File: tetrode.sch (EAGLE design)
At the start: 34 parts, among them IC1 MEGA8-P, J1 AVR_SPI_PROG_3X2NS, U1 LM2576T-5.0/NOPB, Y1 16MHz

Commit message: Started code
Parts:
- removed C5: 22p, resistor:C-EU025-024X044
- removed C6: 470u, resistor:CPOL-EUE5-13
- removed C7: 47u, resistor:CPOL-EUE2.5-6
- removed D2: (no value), adafruit:DIODEDO-1N4148
- removed D3: (no value), adafruit:SCHOTTKY-DIODEDO201T15
- removed L1: 100u, resistor:L-US0204/5
- removed P1, P2, P3: (no value), SparkFun-Connectors:CONN_03
- removed U1: LM2576T-5.0/NOPB, LM2576T:LM2576T-5.0/NOPB
- added J2, J3, J4: (no value), SparkFun-Connectors:CONN_05
- C1: value 47u -> 2.2u; device resistor:CPOL-EUE2.5-6 -> resistor:CPOL-EUE2-5
- C2: value 470u -> 2.2u; device resistor:CPOL-EUE5-13 -> resistor:CPOL-EUE2-5
- C4: value 22p -> 2.2u; device resistor:C-EU025-024X044 -> resistor:CPOL-EUE2-5
- Y1: value 16MHz -> (none); device SparkFun-Clocks:CRYSTAL-16MHZPTH-HC49US -> SparkFun-Clocks:RESONATORPTH-7.6X3.8
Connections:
- removed net N$5: IC1.PC2(ADC2), P3.2
- removed net N$8: D3.C, L1.2, U1.OUT
- removed net VCC: C1.+, C7.+, D2.C, U1.VIN
- net +5V: now also CN1.PWR, J2.1, J3.1, J4.1; no longer C2.+, C6.+, L1.1, P1.1, P2.1, P3.1, U1.FB
- net GND: now also C4.-, J2.5, J3.5, J4.5, Y1.2; no longer C4.2, C5.2, C6.-, C7.-, D3.A, P1.3, P2.3, P3.3, U1.!ON/OFF, U1.GND
- net N$1: now also IC1.PC0(ADC0), J2.3; no longer CN1.PWR, D2.A
- net N$3: now also IC1.PC1(ADC1), J3.3; no longer IC1.PC0(ADC0), P1.2
- net N$4: now also IC1.PC2(ADC2), J4.3; no longer IC1.PC1(ADC1), P2.2
- net SW1: now also C1.+
- net SW2: now also C2.+
- net SW3: now also C4.+
- net XTAL1: no longer C4.1
- net XTAL2: now also Y1.3; no longer C5.1, Y1.2
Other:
- moved on the sheet: C1, C2, S2, S3, S4

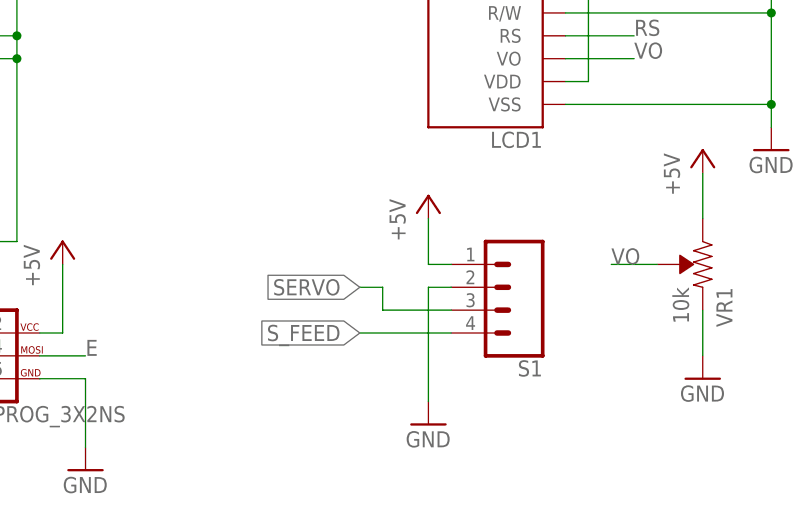
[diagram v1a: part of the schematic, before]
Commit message: Updates to CAD for board and base, started on code
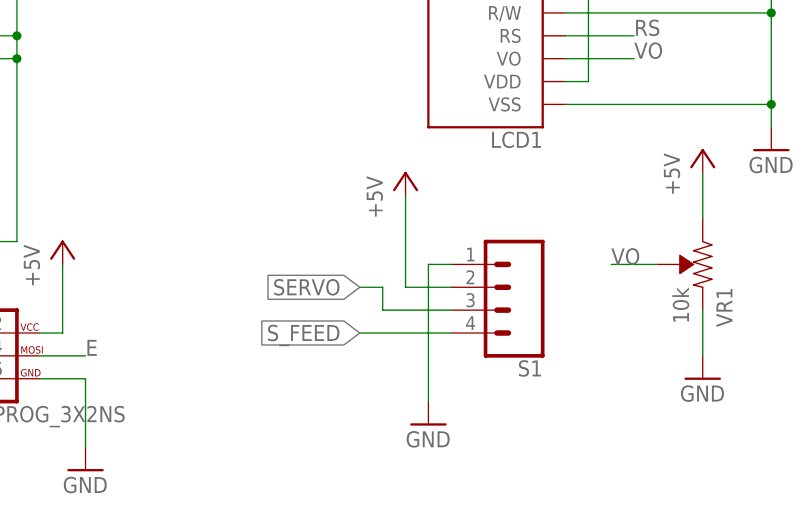
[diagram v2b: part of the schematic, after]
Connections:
- net +5V: now also S1.2; no longer S1.1
- net GND: now also S1.1; no longer S1.2
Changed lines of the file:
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@@
 <part name="P+6" library="supply1" library_urn="urn:adsk.eagle:library:371" deviceset="+5V" device=""/>
 <part name="R3" library="resistor" library_urn="urn:adsk.eagle:library:348" deviceset="R-US_" device="0204/5" package3d_urn="urn:adsk.eagle:package:25955/1" value="220"/>
-<part name="P+7" library="supply1" library_urn="urn:adsk.eagle:library:371" deviceset="+5V" device=""/>
 <part name="GND7" library="supply1" library_urn="urn:adsk.eagle:library:371" deviceset="GND" device=""/>
 <part name="GND8" library="supply1" library_urn="urn:adsk.eagle:library:371" deviceset="GND" device=""/>
@@
 <part name="Y1" library="SparkFun-Clocks" library_urn="urn:adsk.eagle:library:511" deviceset="RESONATOR" device="PTH-7.6X3.8" package3d_urn="urn:adsk.eagle:package:37527/1"/>
 <part name="GND11" library="supply1" library_urn="urn:adsk.eagle:library:371" deviceset="GND" device=""/>
+<part name="P+7" library="supply1" library_urn="urn:adsk.eagle:library:371" deviceset="+5V" device=""/>
 </parts>
 <sheets>
@@
 <attribute name="VALUE" x="66.802" y="156.21" size="1.778" layer="96" rot="R90"/>
 </instance>
-<instance part="P+7" gate="1" x="180.34" y="50.8" smashed="yes">
-<attribute name="VALUE" x="177.8" y="45.72" size="1.778" layer="96" rot="R90"/>
-</instance>
 <instance part="GND7" gate="1" x="180.34" y="25.4" smashed="yes">
 <attribute name="VALUE" x="177.8" y="22.86" size="1.778" layer="96"/>
@@
 <instance part="GND11" gate="1" x="30.48" y="20.32" smashed="yes">
 <attribute name="VALUE" x="27.94" y="17.78" size="1.778" layer="96"/>
+</instance>
+<instance part="P+7" gate="1" x="177.8" y="53.34" smashed="yes">
+<attribute name="VALUE" x="175.26" y="48.26" size="1.778" layer="96" rot="R90"/>
 </instance>
 </instances>
@@
 <pinref part="R3" gate="G$1" pin="2"/>
 <wire x1="63.5" y1="172.72" x2="63.5" y2="165.1" width="0.1524" layer="91"/>
-</segment>
-<segment>
-<pinref part="S1" gate="G$1" pin="1"/>
-<pinref part="P+7" gate="1" pin="+5V"/>
-<wire x1="182.88" y1="43.18" x2="180.34" y2="43.18" width="0.1524" layer="91"/>
-<wire x1="180.34" y1="43.18" x2="180.34" y2="48.26" width="0.1524" layer="91"/>
 </segment>
 <segment>
@@
 <wire x1="101.6" y1="101.6" x2="101.6" y2="124.46" width="0.1524" layer="91"/>
 <junction x="101.6" y="124.46"/>
+</segment>
+<segment>
+<pinref part="S1" gate="G$1" pin="2"/>
+<wire x1="182.88" y1="40.64" x2="177.8" y2="40.64" width="0.1524" layer="91"/>
+<pinref part="P+7" gate="1" pin="+5V"/>
+<wire x1="177.8" y1="40.64" x2="177.8" y2="50.8" width="0.1524" layer="91"/>
 </segment>
 </net>
@@
 </segment>
 <segment>
-<pinref part="S1" gate="G$1" pin="2"/>
-<pinref part="GND7" gate="1" pin="GND"/>
-<wire x1="182.88" y1="40.64" x2="180.34" y2="40.64" width="0.1524" layer="91"/>
-<wire x1="180.34" y1="40.64" x2="180.34" y2="27.94" width="0.1524" layer="91"/>
-</segment>
-<segment>
 <pinref part="GND8" gate="1" pin="GND"/>
 <wire x1="218.44" y1="58.42" x2="218.44" y2="60.96" width="0.1524" layer="91"/>
@@
 <wire x1="30.48" y1="30.48" x2="30.48" y2="22.86" width="0.1524" layer="91"/>
 </segment>
+<segment>
+<pinref part="GND7" gate="1" pin="GND"/>
+<wire x1="180.34" y1="27.94" x2="180.34" y2="43.18" width="0.1524" layer="91"/>
+<pinref part="S1" gate="G$1" pin="1"/>
+<wire x1="180.34" y1="43.18" x2="182.88" y2="43.18" width="0.1524" layer="91"/>
+</segment>
 </net>

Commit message: Switched layout of board and reduced max speed of servo to resolve brown out when the servo stops
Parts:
- removed Y1: (no value), SparkFun-Clocks:RESONATORPTH-7.6X3.8
- added C5: 47u, resistor:CPOL-EUE2.5-6
- J2, J3, J4: device SparkFun-Connectors:CONN_05 -> SparkFun-Connectors:CONN_03
- R1, R2, R3, R4, R5, R6, R7, R8: device resistor:R-US_0204/5 -> resistor:R-US_0309/10
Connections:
- removed net N$4: IC1.PC2(ADC2), J4.3
- removed net XTAL1: IC1.PB6(XTAL1/TOSC1), Y1.1
- removed net XTAL2: IC1.PB7(XTAL2/TOSC2), Y1.3
- new net N$5: IC1.PC2(ADC2), J4.2
- net +5V: now also C5.+
- net GND: now also C5.-, J2.3, J3.3, J4.3; no longer J2.5, J3.5, J4.5, Y1.2
- net N$1: now also J2.2; no longer J2.3
- net N$3: now also J3.2; no longer J3.3
